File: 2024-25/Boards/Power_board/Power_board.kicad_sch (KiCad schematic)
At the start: 29 parts, among them J2 0430451212, Q1 AON6411, Q2 AON6411, Q3 AON6411, Q4 DMN2056U, Q5 DMN2056U, Q6 DMN2056U

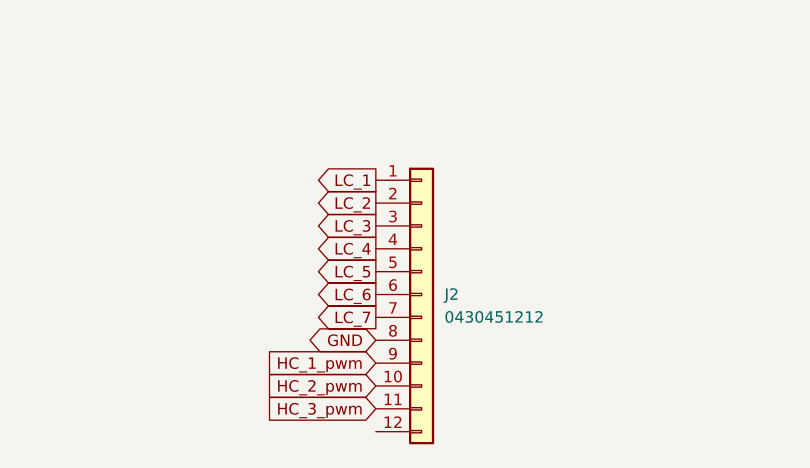
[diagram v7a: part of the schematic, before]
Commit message: made connector dnp
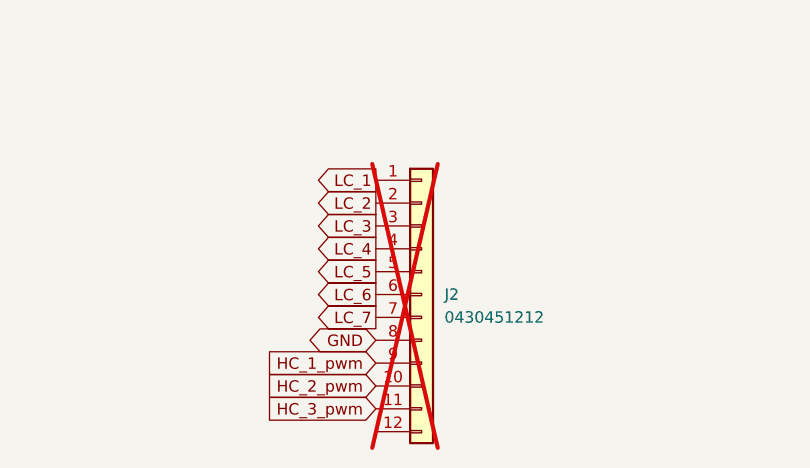
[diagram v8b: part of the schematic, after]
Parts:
- J2: now not fitted
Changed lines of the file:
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@@
 		(in_bom yes)
 		(on_board yes)
-		(dnp no)
+		(dnp yes)
 		(fields_autoplaced yes)
 		(property "Reference" "J2"
